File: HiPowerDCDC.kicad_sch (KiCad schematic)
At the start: 66 parts, among them J1 Conn_01x01, J2 Conn_01x01, J3 Conn_01x01, J4 Conn_01x01, J5 Conn_01x04, Q1 WMJ38N60, Q2 WMJ38N60, SW1 SW_Push, SW2 SW_Push, U1 ESP32-WROOM-32U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

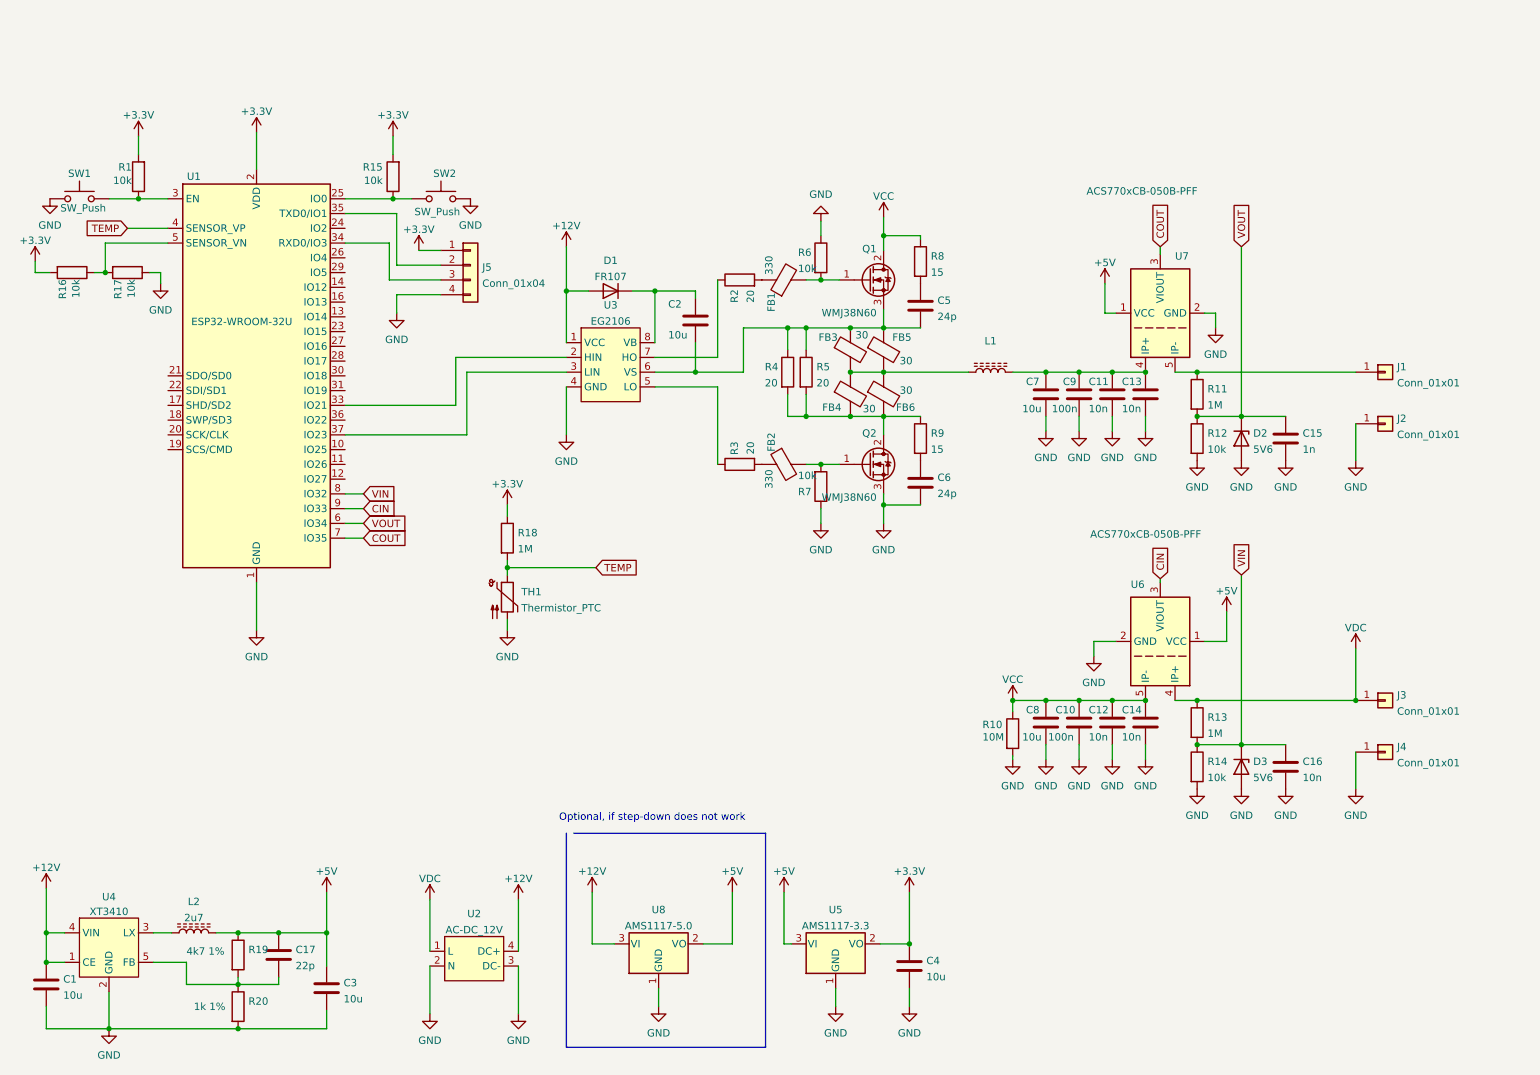
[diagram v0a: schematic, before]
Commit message: Changed ACS770 to CC6900
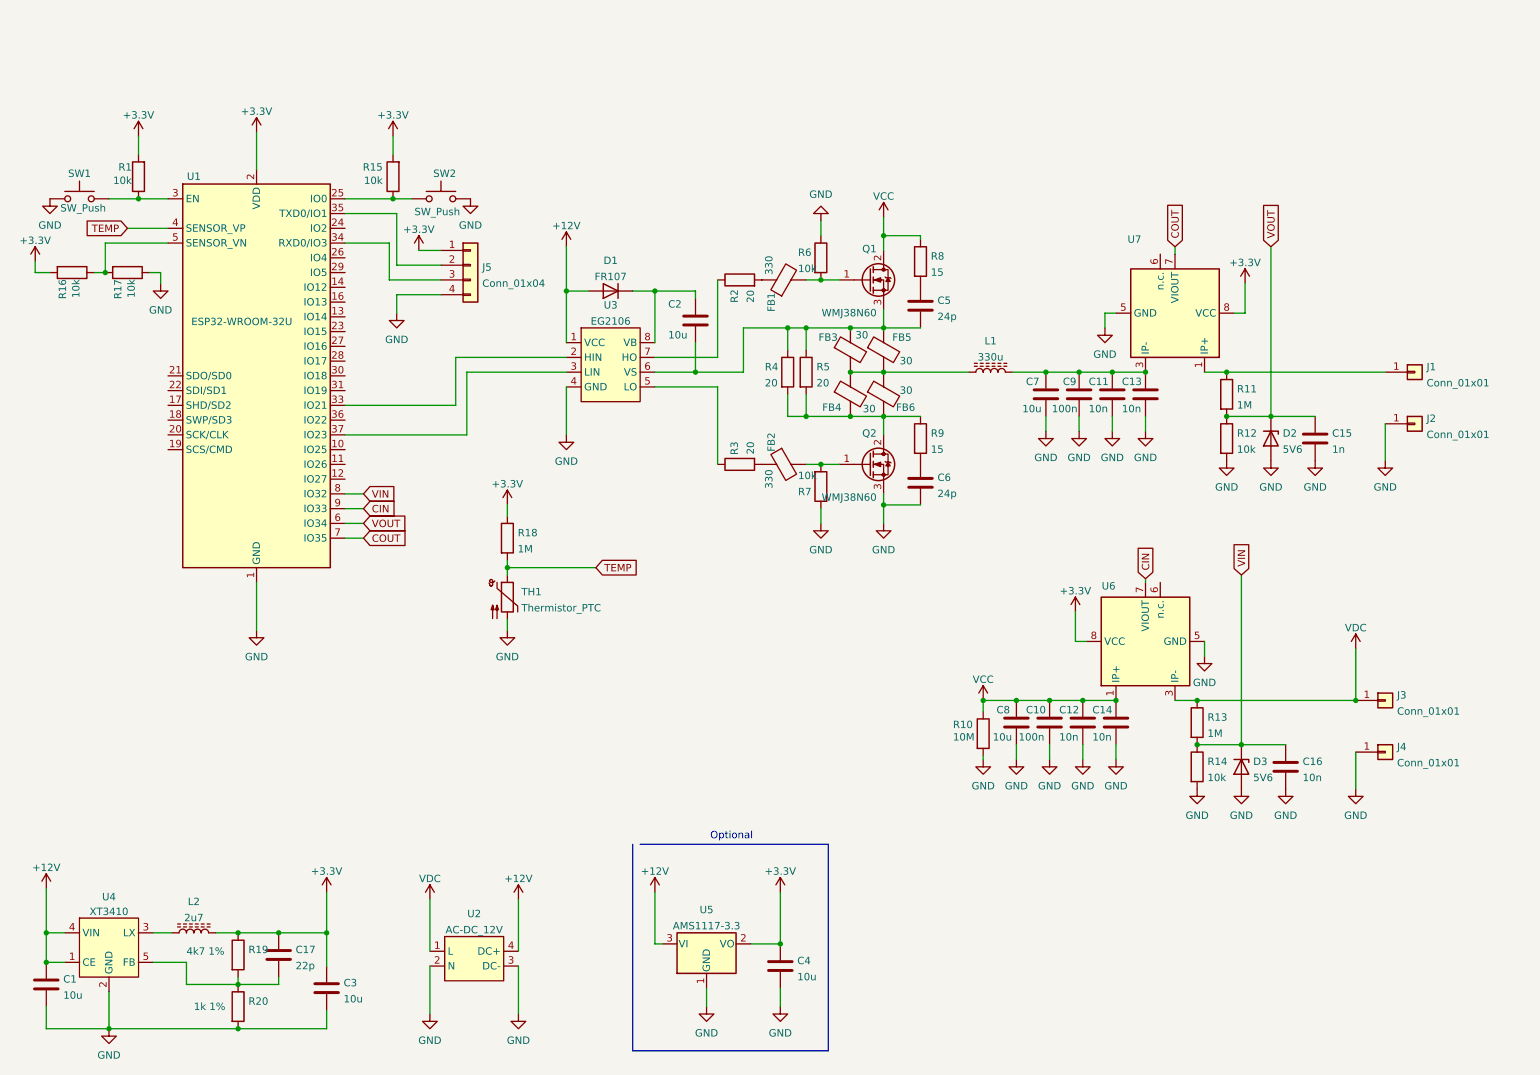
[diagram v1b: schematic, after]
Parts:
- removed U6, U7: ACS770xCB-050B-PFF, Sensor_Current:Allegro_CB_PFF, symbol Sensor_Current:ACS770xCB-050B-PFF
- removed U8: AMS1117-5.0, Package_TO_SOT_SMD:SOT-223-3_TabPin2, symbol Regulator_Linear:AMS1117-5.0
- added U6, U7: (no value), symbol SolarLibrary:CC6903SO-20A
- L1: value (none) -> 330u; footprint (none) -> HiPowerFP:L_Toroid_Vertical_L54.0mm_W23.8mm_P20.10mm_Bourns_5700
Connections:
- net +12V: now also U5.3 (VI)
- net +3V3: now also C17.1, C3.1, L2.2, R19.1, U6.8 (VCC), U7.8 (VCC)
- net CIN: now also U6.7 (VIOUT)
- net COUT: now also U7.7 (VIOUT)
- net GND: now also U6.5 (GND), U7.5 (GND)
- net VCC: now also U6.1 (IP+), U6.2 (IP+)
- net VDC: now also U6.3 (IP-), U6.4 (IP-)
- net at C11.1, C13.1, C7.1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: now also U7.3 (IP-), U7.4 (IP-)
- net at J1.1 (Pin_1), R11.1: now also U7.1 (IP+), U7.2 (IP+)
- removed net +5V: C17.1, C3.1, L2.2, R19.1, U5.3 (VI)
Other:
- note added: "Optional"
- note removed: "Optional, if step-down does not work"
- moved on the sheet: C10, C12, C14, C15, C4, C8, D2, J1, J2, R10, R11, R12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

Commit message: Added logos and 3V3 enable pin
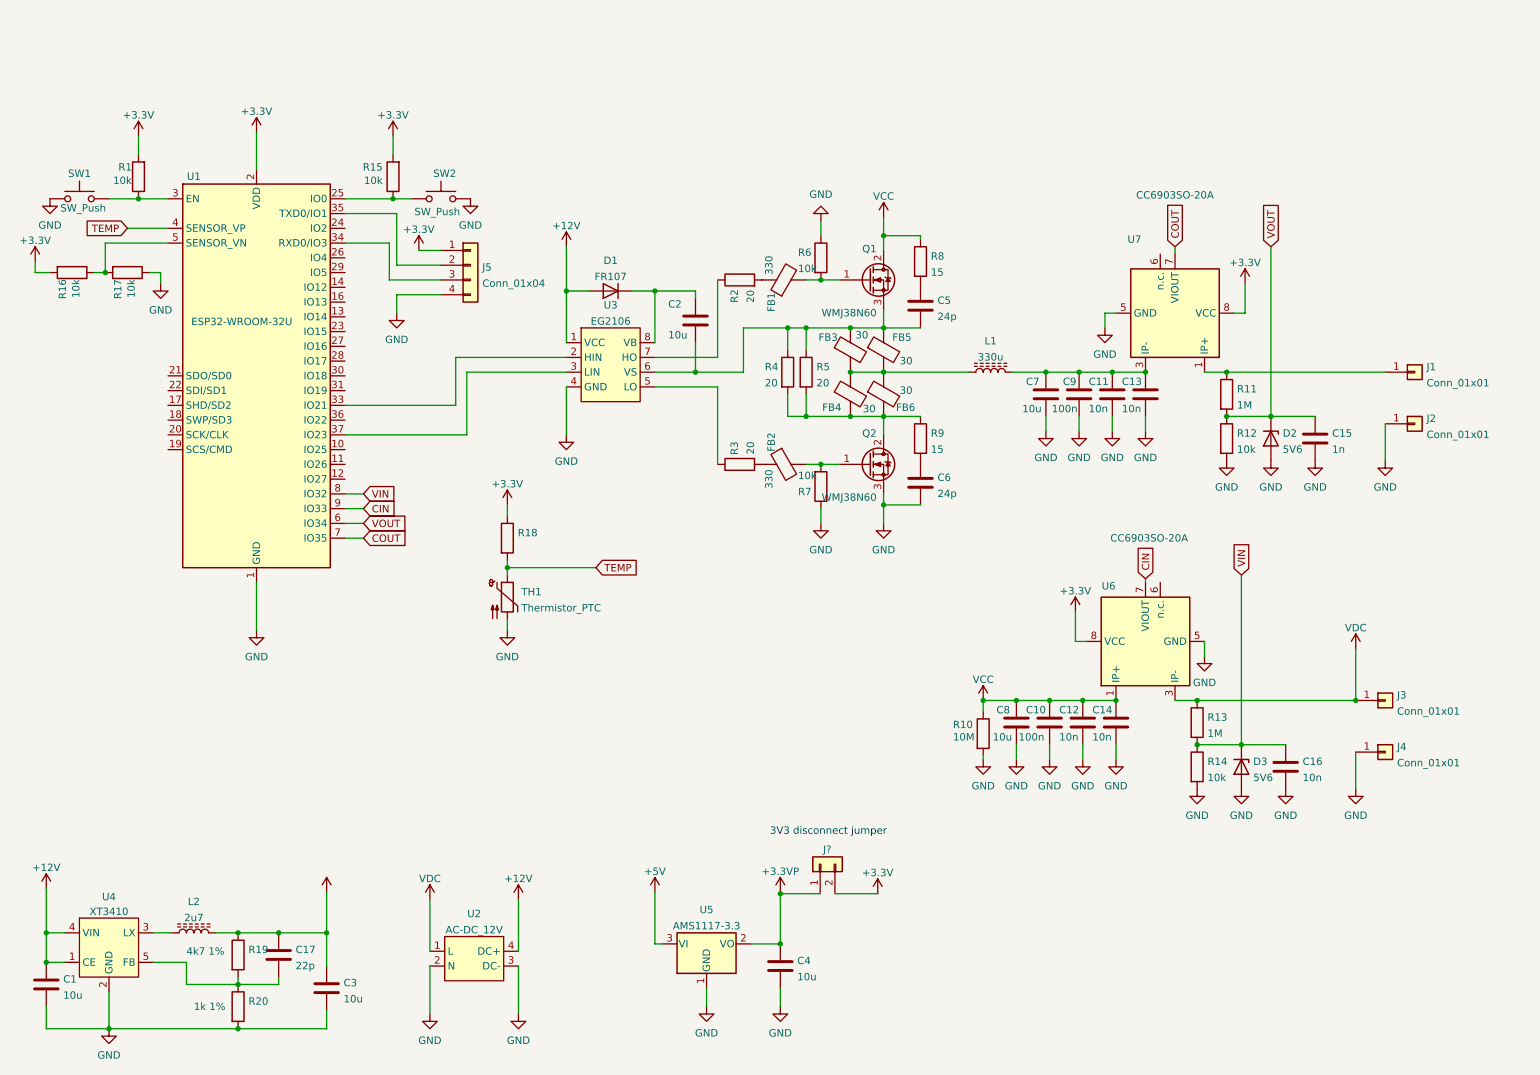
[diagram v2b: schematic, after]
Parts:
- added J?: (no value), symbol Connector_Generic:Conn_01x02
- R18: value 1M -> (none); footprint Resistor_SMD:R_1206_3216Metric -> (none)
- U6, U7: value (none) -> CC6903SO-20A; footprint (none) -> Package_SO:SO-8_3.9x4.9mm_P1.27mm
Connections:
- net +12V: no longer U5.3 (VI)
- net +3V3: now also J?.2 (Pin_2); no longer C17.1, C3.1, C4.1, L2.2, R19.1, U5.2 (VO)
- new net +3.3VP: C4.1, J?.1 (Pin_1), U5.2 (VO)
- new net +5V: C17.1, C3.1, L2.2, R19.1, U5.3 (VI)
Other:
- note added: "3V3 disconnect jumper"
- note removed: "Optional"

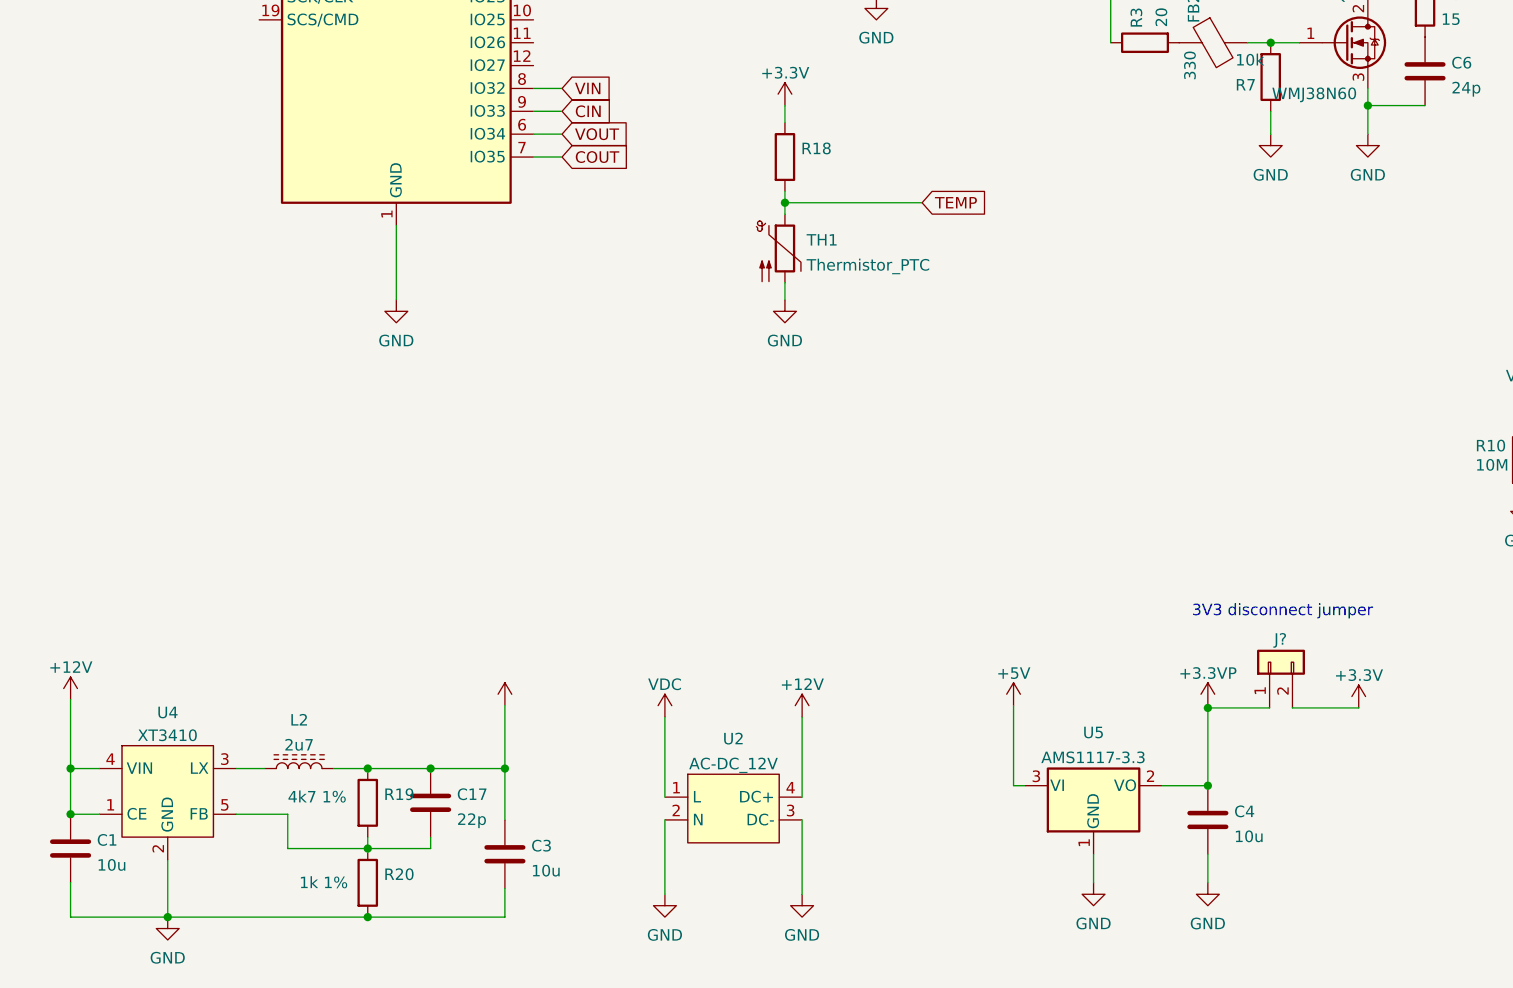
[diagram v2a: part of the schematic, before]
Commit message: Added fan output and changed XT3410 to SD8942
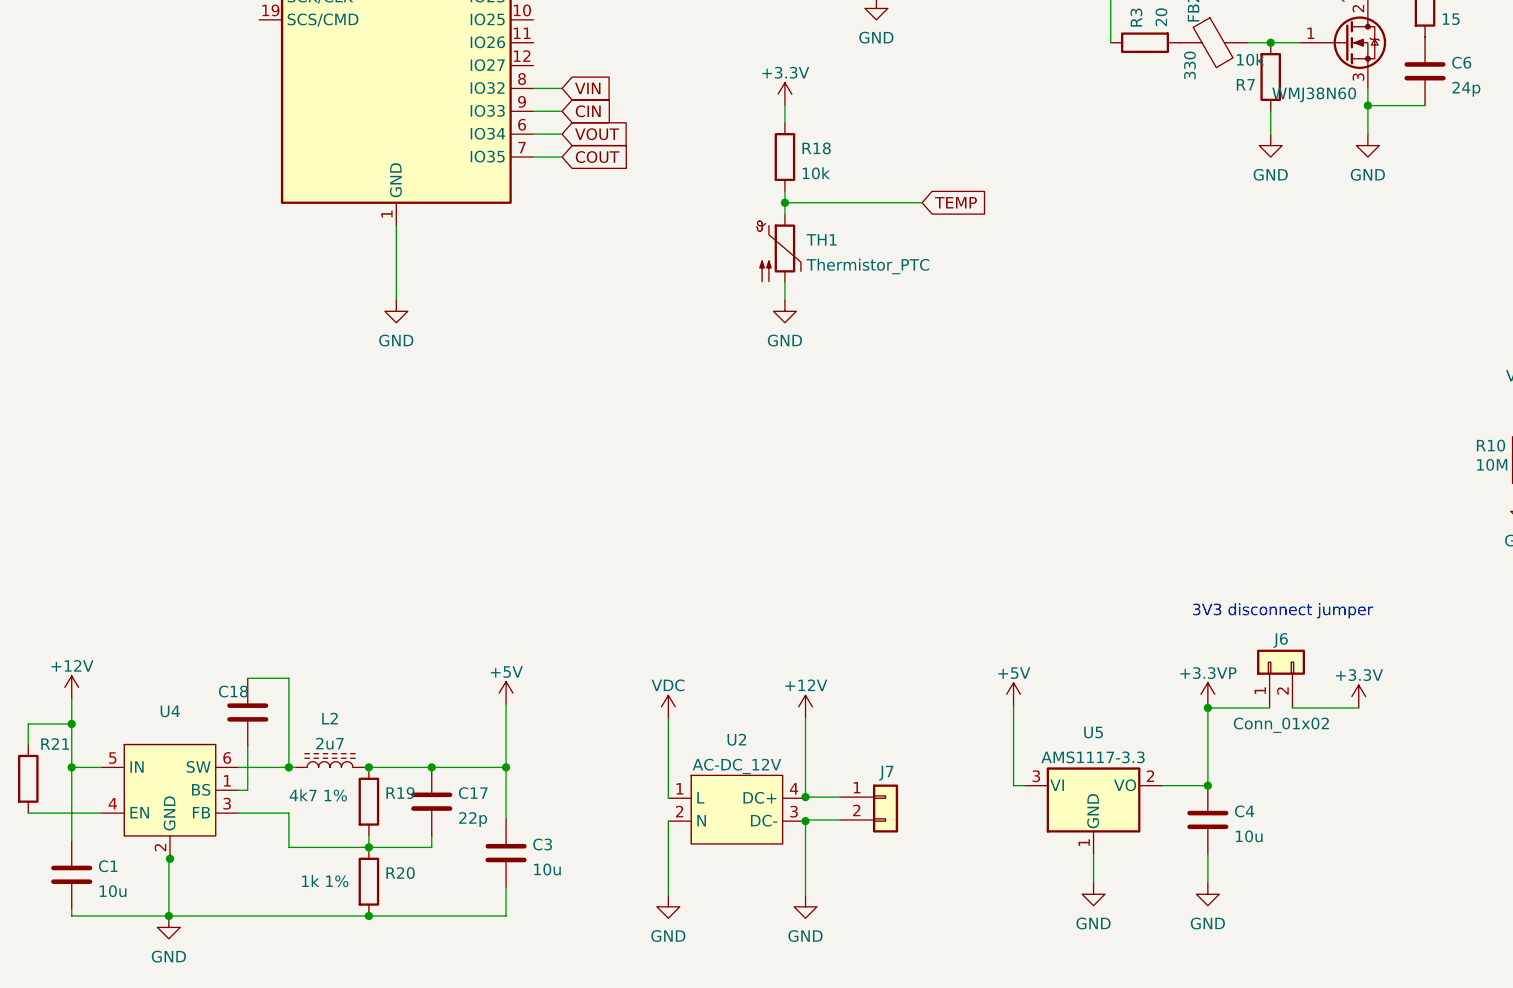
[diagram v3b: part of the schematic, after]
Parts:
- removed U4: XT3410, Package_TO_SOT_SMD:SOT-23-5, symbol SolarLibrary:XT3410
- added C18: (no value), symbol Device:C
- added J7: (no value), Connector_PinHeader_2.54mm:PinHeader_1x02_P2.54mm_Vertical, symbol Connector_Generic:Conn_01x02
- added R21: (no value), symbol Device:R
- added U4: (no value), symbol SolarLibrary:SD8942
- J6: renamed from J?; value (none) -> Conn_01x02; footprint (none) -> Connector_PinHeader_2.54mm:PinHeader_1x02_P2.54mm_Vertical
- R18: value (none) -> 10k; footprint (none) -> Resistor_SMD:R_1206_3216Metric
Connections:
- net +12V: now also J7.1 (Pin_1), R21.1, U4.5 (IN)
- net GND: now also J7.2 (Pin_2)
- net at C17.2, R19.2, R20.1: now also U4.3 (FB)
- net at L2.1: now also C18.1, U4.6 (SW)
- new net: C18.2, U4.1 (BS)
- new net: R21.2, U4.4 (EN)
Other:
- moved on the sheet: C1, L2
